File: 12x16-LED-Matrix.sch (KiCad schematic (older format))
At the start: 197 parts, among them J1 Conn_01x16, J2 Conn_01x12

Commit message: Add ground pins, fix silkscreen
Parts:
- removed J1: Conn_01x16, Connector_PinHeader_2.54mm:PinHeader_1x16_P2.54mm_Vertical, symbol Connector_Generic:Conn_01x16
- removed J2: Conn_01x12, Connector_PinHeader_2.54mm:PinHeader_1x12_P2.54mm_Vertical, symbol Connector_Generic:Conn_01x12
- added J1: Conn_01x17, Connector_PinHeader_2.54mm:PinHeader_1x17_P2.54mm_Vertical, symbol Connector_Generic:Conn_01x17
- added J2: Conn_01x13, Connector_PinHeader_2.54mm:PinHeader_1x13_P2.54mm_Vertical, symbol Connector_Generic:Conn_01x13
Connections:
- net at D1.1 (K), D10.1 (K), D11.1 (K)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: now also J2.12 (Pin_12)
- net at D114.2 (A), D130.2 (A), D146.2 (A)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: now also J1.2 (Pin_2)
- net at D115.2 (A), D131.2 (A), D147.2 (A)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: now also J1.3 (Pin_3)
- net at D100.2 (A), D116.2 (A), D132.2 (A)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: now also J1.4 (Pin_4)
- net at D101.2 (A), D117.2 (A), D133.2 (A)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: now also J1.5 (Pin_5)
- net at D102.2 (A), D118.2 (A), D134.2 (A)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: now also J1.6 (Pin_6)
- net at D103.2 (A), D119.2 (A), D135.2 (A)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: now also J1.7 (Pin_7)
- net at D104.2 (A), D120.2 (A), D136.2 (A)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: now also J1.8 (Pin_8)
- net at D105.2 (A), D121.2 (A), D137.2 (A)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: now also J1.9 (Pin_9)
- net at D10.2 (A), D106.2 (A), D122.2 (A)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: now also J1.10 (Pin_10)
- net at D107.2 (A), D11.2 (A), D123.2 (A)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: now also J1.11 (Pin_11)
- net at D108.2 (A), D12.2 (A), D124.2 (A)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: now also J1.12 (Pin_12)
- net at D109.2 (A), D125.2 (A), D13.2 (A)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: now also J1.13 (Pin_13)
- net at D110.2 (A), D126.2 (A), D14.2 (A)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: now also J1.14 (Pin_14)
- net at D111.2 (A), D127.2 (A), D143.2 (A)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: now also J1.15 (Pin_15)
- net at D112.2 (A), D128.2 (A), D144.2 (A)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: now also J1.16 (Pin_16)
- net at D1.2 (A), D113.2 (A), D129.2 (A)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: now also J1.1 (Pin_1)
- net at D17.1 (K), D18.1 (K), D19.1 (K)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: now also J2.11 (Pin_11)
- net at D33.1 (K), D34.1 (K), D35.1 (K)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: now also J2.10 (Pin_10)
- net at D49.1 (K), D50.1 (K), D51.1 (K)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: now also J2.9 (Pin_9)
- net at D65.1 (K), D66.1 (K), D67.1 (K)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: now also J2.8 (Pin_8)
- net at D81.1 (K), D82.1 (K), D83.1 (K)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: now also J2.7 (Pin_7)
- net at D100.1 (K), D101.1 (K), D102.1 (K)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: now also J2.6 (Pin_6)
- net at D113.1 (K), D114.1 (K), D115.1 (K)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: now also J2.5 (Pin_5)
- net at D129.1 (K), D130.1 (K), D131.1 (K)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: now also J2.4 (Pin_4)
- net at D145.1 (K), D146.1 (K), D147.1 (K)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: now also J2.3 (Pin_3)
- net at D161.1 (K), D162.1 (K), D163.1 (K)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: now also J2.2 (Pin_2)
- net at D177.1 (K), D178.1 (K), D179.1 (K)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: now also J2.1 (Pin_1)
- new net GND: J1.17 (Pin_17), J2.13 (Pin_13)
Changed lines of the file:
@@
 Wire Wire Line
 	6200 5500 6200 5150
-$Comp
-L Connector_Generic:Conn_01x12 J2
-U 1 1 61F0FCFB
-P 750 2700
-F 0 "J2" H 668 1875 50  0000 C CNN
-F 1 "Conn_01x12" H 668 1966 50  0000 C CNN
-F 2 "Connector_PinHeader_2.54mm:PinHeader_1x12_P2.54mm_Vertical" H 750 2700 50  0001 C CNN
-F 3 "~" H 750 2700 50  0001 C CNN
-	1    750  2700
-	-1   0    0    1
-$EndComp
 Wire Wire Line
 	1500 2450 1450 2450
@@
 	1500 2100 950  2100
 Connection ~ 1500 2100
-$Comp
-L Connector_Generic:Conn_01x16 J1
-U 1 1 62BDBE0D
-P 2400 850
-F 0 "J1" V 2617 796 50  0000 C CNN
-F 1 "Conn_01x16" V 2526 796 50  0000 C CNN
-F 2 "Connector_PinHeader_2.54mm:PinHeader_1x16_P2.54mm_Vertical" H 2400 850 50  0001 C CNN
-F 3 "~" H 2400 850 50  0001 C CNN
-	1    2400 850
-	0    -1   -1   0
-$EndComp
-Wire Wire Line
-	1700 1050 1700 2000
 Wire Wire Line
 	2000 1750 1800 1750
@@
 	5900 1100 3100 1100
 Wire Wire Line
-	3100 1100 3100 1050
-Wire Wire Line
 	5900 1100 5900 2000
 Wire Wire Line
-	6200 1050 3200 1050
-Wire Wire Line
 	6200 1050 6200 2000
-Wire Wire Line
-	3000 1050 3000 1150
-Wire Wire Line
-	2900 1050 2900 1200
-Wire Wire Line
-	2800 1050 2800 1250
-Wire Wire Line
-	2700 1050 2700 1300
-Wire Wire Line
-	2600 1050 2600 1350
-Wire Wire Line
-	2500 1050 2500 1400
-Wire Wire Line
-	2400 1050 2400 1450
-Wire Wire Line
-	2300 1050 2300 1500
-Wire Wire Line
-	2200 1050 2200 1550
-Wire Wire Line
-	2100 1050 2100 1600
-Wire Wire Line
-	2000 1050 2000 1650
-Wire Wire Line
-	1900 1050 1900 1700
-Wire Wire Line
-	1800 1050 1800 1750
 $Comp
 L Mechanical:MountingHole H1
@@
 	1    0    0    -1
 $EndComp
+$Comp
+L Connector_Generic:Conn_01x13 J2
+U 1 1 61961DD2
+P 750 2600
+F 0 "J2" H 668 1775 50  0000 C CNN
+F 1 "Conn_01x13" H 668 1866 50  0000 C CNN
+F 2 "Connector_PinHeader_2.54mm:PinHeader_1x13_P2.54mm_Vertical" H 750 2600 50  0001 C CNN
+F 3 "~" H 750 2600 50  0001 C CNN
+	1    750  2600
+	-1   0    0    1
+$EndComp
+$Comp
+L power:GND #PWR0101
+U 1 1 619641D7
+P 950 2000
+F 0 "#PWR0101" H 950 1750 50  0001 C CNN
+F 1 "GND" V 955 1872 50  0000 R CNN
+F 2 "" H 950 2000 50  0001 C CNN
+F 3 "" H 950 2000 50  0001 C CNN
+	1    950  2000
+	0    -1   -1   0
+$EndComp
+$Comp
+L Connector_Generic:Conn_01x17 J1
+U 1 1 61965EDC
+P 2500 800
+F 0 "J1" V 2717 796 50  0000 C CNN
+F 1 "Conn_01x17" V 2626 796 50  0000 C CNN
+F 2 "Connector_PinHeader_2.54mm:PinHeader_1x17_P2.54mm_Vertical" H 2500 800 50  0001 C CNN
+F 3 "~" H 2500 800 50  0001 C CNN
+	1    2500 800
+	0    -1   -1   0
+$EndComp
+Wire Wire Line
+	3200 1050 3200 1000
+Wire Wire Line
+	3200 1050 6200 1050
+Wire Wire Line
+	3100 1000 3100 1100
+Wire Wire Line
+	3000 1000 3000 1150
+Wire Wire Line
+	2900 1000 2900 1200
+Wire Wire Line
+	2800 1000 2800 1250
+Wire Wire Line
+	2700 1000 2700 1300
+Wire Wire Line
+	2600 1000 2600 1350
+Wire Wire Line
+	2500 1000 2500 1400
+Wire Wire Line
+	2400 1000 2400 1450
+Wire Wire Line
+	2300 1000 2300 1500
+Wire Wire Line
+	2200 1000 2200 1550
+Wire Wire Line
+	2100 1000 2100 1600
+Wire Wire Line
+	2000 1000 2000 1650
+Wire Wire Line
+	1900 1000 1900 1700
+Wire Wire Line
+	1800 1000 1800 1750
+Wire Wire Line
+	1700 1000 1700 2000
+$Comp
+L power:GND #PWR0102
+U 1 1 620A84A1
+P 3300 1000
+F 0 "#PWR0102" H 3300 750 50  0001 C CNN
+F 1 "GND" V 3305 872 50  0000 R CNN
+F 2 "" H 3300 1000 50  0001 C CNN
+F 3 "" H 3300 1000 50  0001 C CNN
+	1    3300 1000
+	0    -1   -1   0
+$EndComp
 $EndSCHEMATC

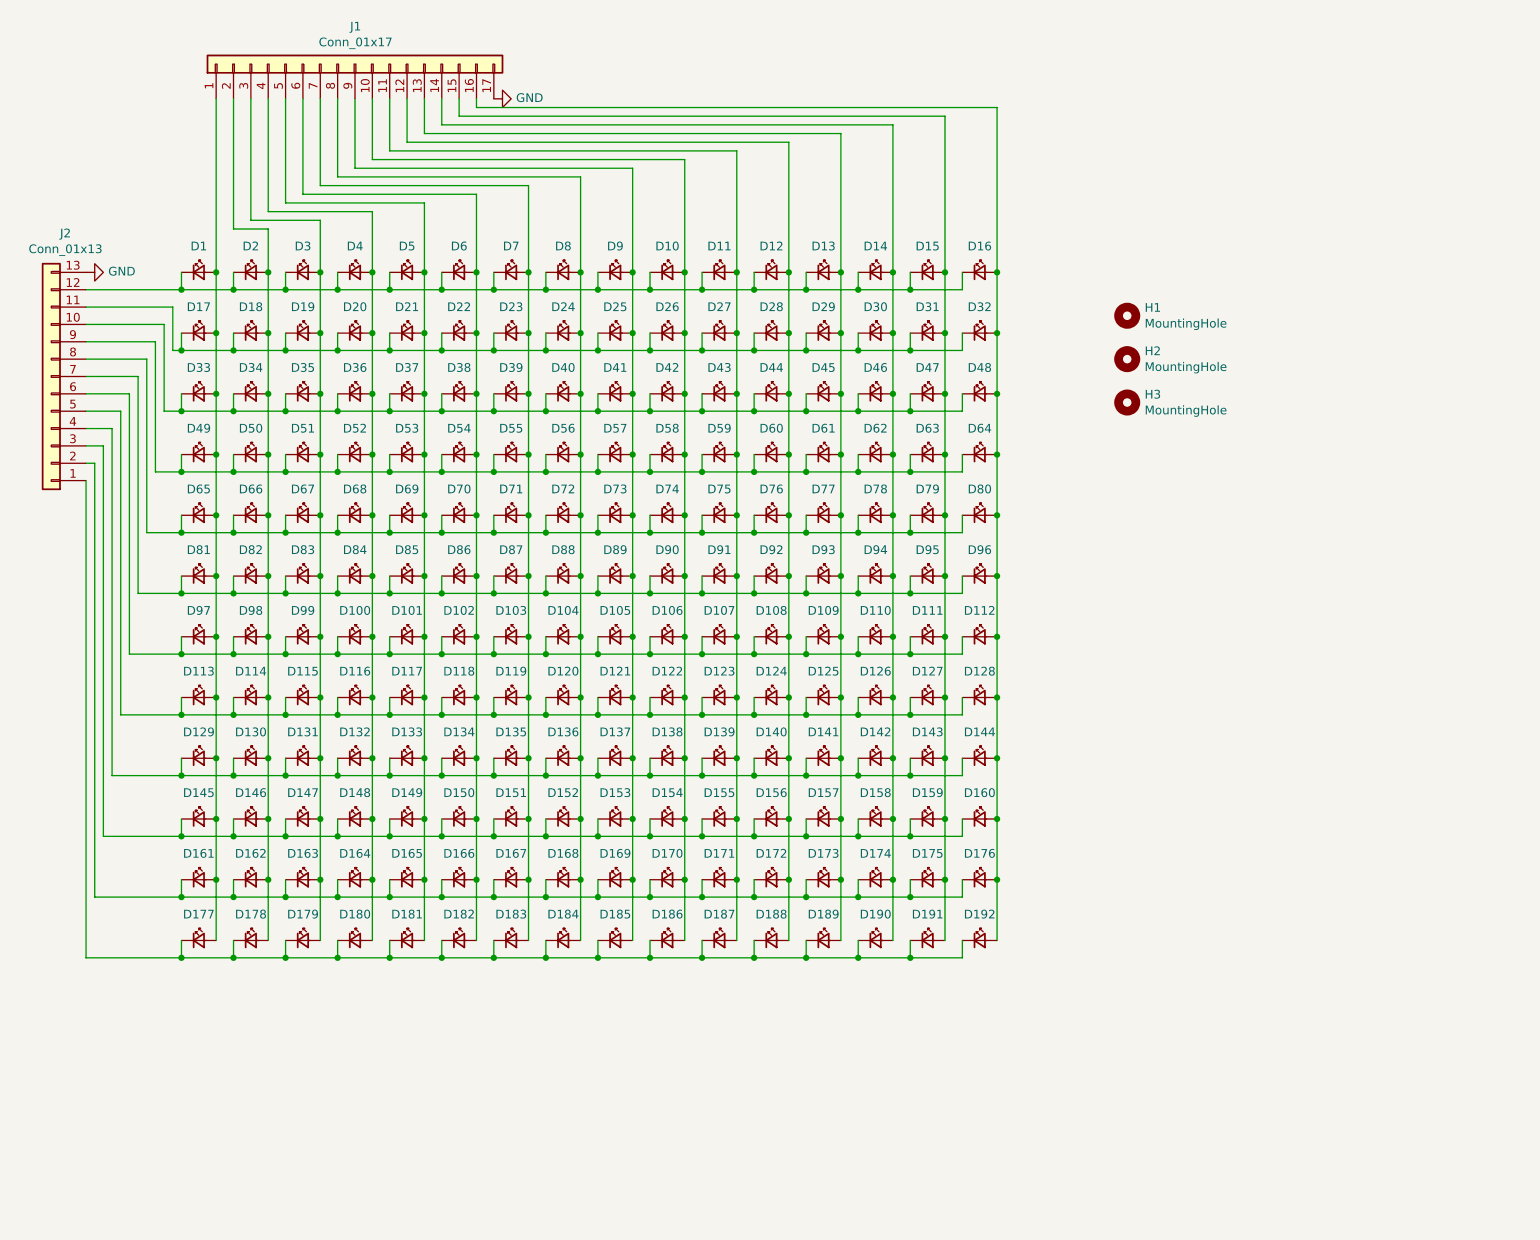
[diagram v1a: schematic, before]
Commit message: Add driver directly to schematic
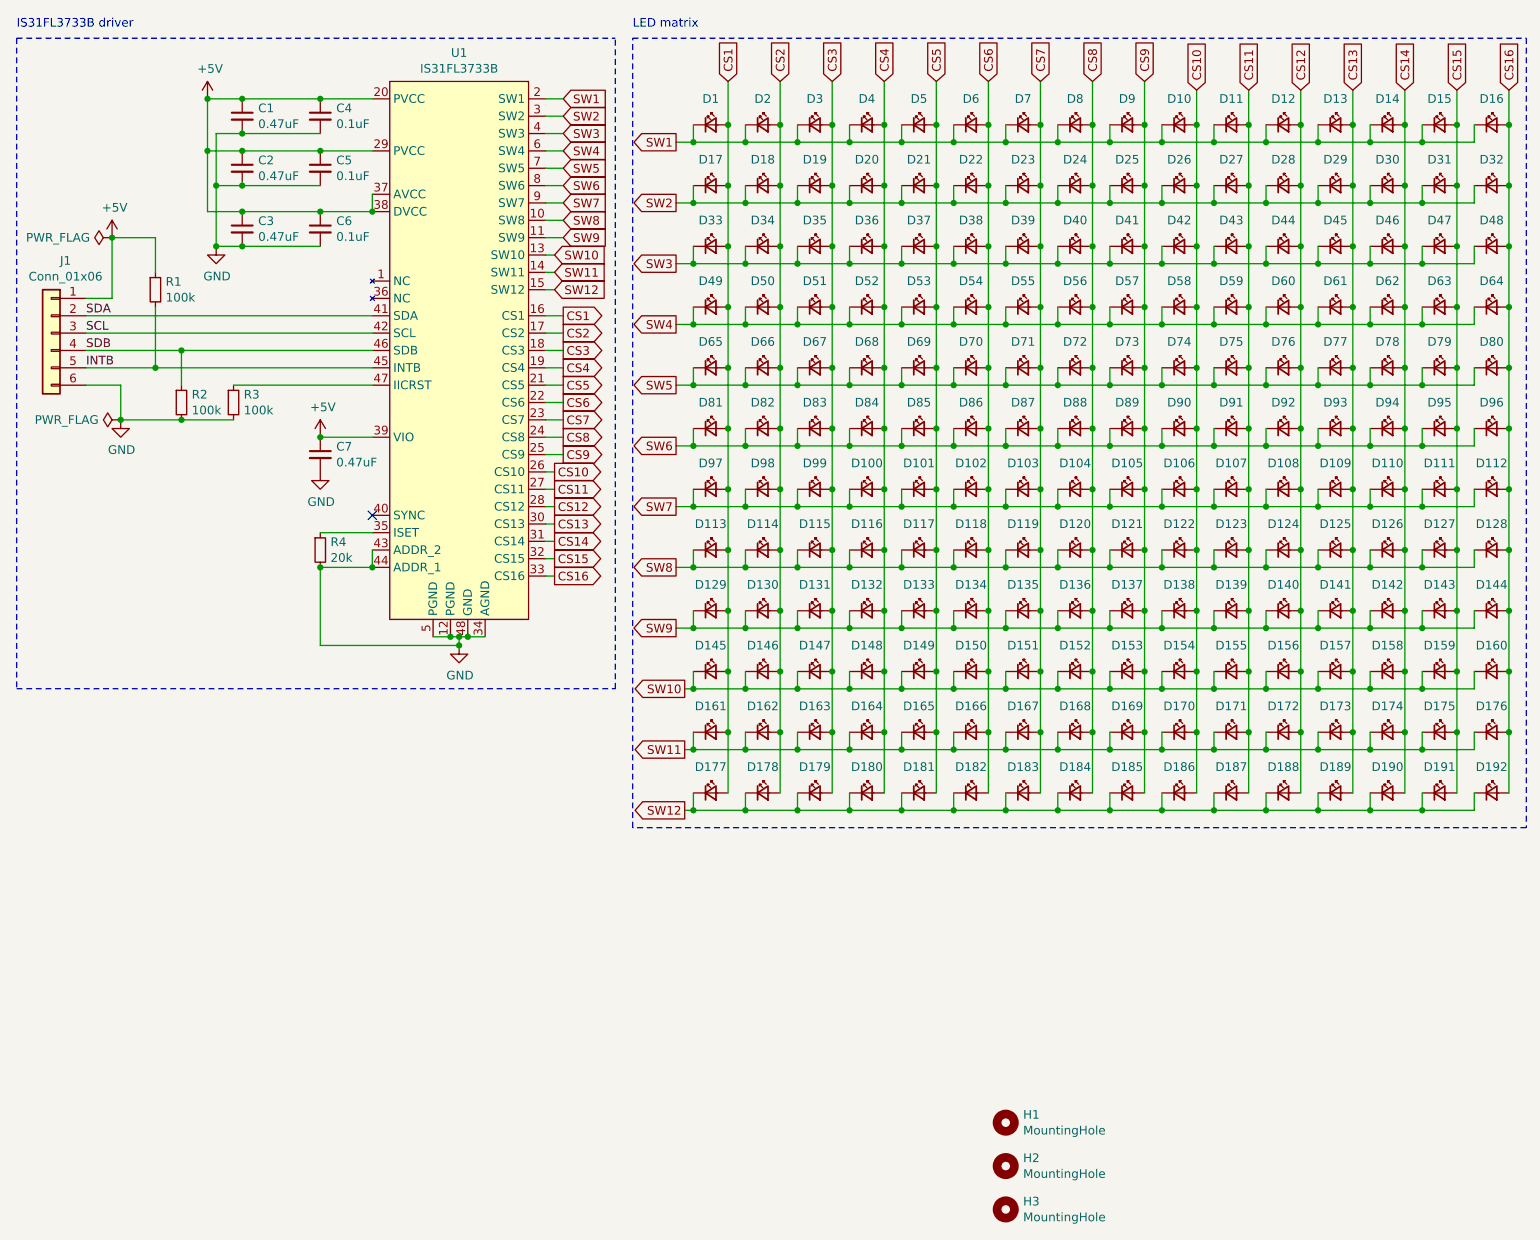
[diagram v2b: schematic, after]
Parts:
- removed J1: Conn_01x17, Connector_PinHeader_2.54mm:PinHeader_1x17_P2.54mm_Vertical, symbol Connector_Generic:Conn_01x17
- removed J2: Conn_01x13, Connector_PinHeader_2.54mm:PinHeader_1x13_P2.54mm_Vertical, symbol Connector_Generic:Conn_01x13
- added C1, C2, C3, C7: 0.47uF, Capacitor_SMD:C_0402_1005Metric, symbol Device:C_Small
- added C4, C5, C6: 0.1uF, Capacitor_SMD:C_0402_1005Metric, symbol Device:C_Small
- added J1: Conn_01x06, Connector_PinHeader_2.54mm:PinHeader_1x06_P2.54mm_Vertical, symbol Connector_Generic:Conn_01x06
- added R1, R2, R3: 100k, Resistor_SMD:R_0402_1005Metric, symbol Device:R_Small
- added R4: 20k, Resistor_SMD:R_0402_1005Metric, symbol Device:R_Small
- added U1: IS31FL3733B, Package_DFN_QFN:QFN-48-1EP_6x6mm_P0.4mm_EP4.3x4.3mm_ThermalVias, symbol 12x16-LED-Matrix:IS31FL3733B
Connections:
- net GND: now also C1.2, C2.2, C3.2, C4.2, C5.2, C6.2, C7.2, J1.6 (Pin_6), R2.2, R3.2, R4.2, U1.12 (PGND), U1.34 (AGND), U1.43 (ADDR_2), U1.44 (ADDR_1), U1.48 (GND), U1.5 (PGND)
- net SW1: now reaches D1.1 (K), D10.1 (K), D11.1 (K), D12.1 (K), D13.1 (K), D14.1 (K), D15.1 (K), D16.1 (K), D2.1 (K), D3.1 (K), D4.1 (K), D5.1 (K), D6.1 (K), D7.1 (K), D8.1 (K), D9.1 (K)
- net SW1: now also U1.2 (SW1)
- net CS2: now reaches D114.2 (A), D130.2 (A), D146.2 (A), D162.2 (A), D178.2 (A), D18.2 (A), D2.2 (A), D34.2 (A), D50.2 (A), D66.2 (A), D82.2 (A), D98.2 (A)
- net CS2: now also U1.17 (CS2)
- net CS3: now reaches D115.2 (A), D131.2 (A), D147.2 (A), D163.2 (A), D179.2 (A), D19.2 (A), D3.2 (A), D35.2 (A), D51.2 (A), D67.2 (A), D83.2 (A), D99.2 (A)
- net CS3: now also U1.18 (CS3)
- net CS4: now reaches D100.2 (A), D116.2 (A), D132.2 (A), D148.2 (A), D164.2 (A), D180.2 (A), D20.2 (A), D36.2 (A), D4.2 (A), D52.2 (A), D68.2 (A), D84.2 (A)
- net CS4: now also U1.19 (CS4)
- net CS5: now reaches D101.2 (A), D117.2 (A), D133.2 (A), D149.2 (A), D165.2 (A), D181.2 (A), D21.2 (A), D37.2 (A), D5.2 (A), D53.2 (A), D69.2 (A), D85.2 (A)
- net CS5: now also U1.21 (CS5)
- net CS6: now reaches D102.2 (A), D118.2 (A), D134.2 (A), D150.2 (A), D166.2 (A), D182.2 (A), D22.2 (A), D38.2 (A), D54.2 (A), D6.2 (A), D70.2 (A), D86.2 (A)
- net CS6: now also U1.22 (CS6)
- net CS7: now reaches D103.2 (A), D119.2 (A), D135.2 (A), D151.2 (A), D167.2 (A), D183.2 (A), D23.2 (A), D39.2 (A), D55.2 (A), D7.2 (A), D71.2 (A), D87.2 (A)
- net CS7: now also U1.23 (CS7)
- net CS8: now reaches D104.2 (A), D120.2 (A), D136.2 (A), D152.2 (A), D168.2 (A), D184.2 (A), D24.2 (A), D40.2 (A), D56.2 (A), D72.2 (A), D8.2 (A), D88.2 (A)
- net CS8: now also U1.24 (CS8)
- net CS9: now reaches D105.2 (A), D121.2 (A), D137.2 (A), D153.2 (A), D169.2 (A), D185.2 (A), D25.2 (A), D41.2 (A), D57.2 (A), D73.2 (A), D89.2 (A), D9.2 (A)
- net CS9: now also U1.25 (CS9)
- net CS10: now reaches D10.2 (A), D106.2 (A), D122.2 (A), D138.2 (A), D154.2 (A), D170.2 (A), D186.2 (A), D26.2 (A), D42.2 (A), D58.2 (A), D74.2 (A), D90.2 (A)
- net CS10: now also U1.26 (CS10)
- net CS11: now reaches D107.2 (A), D11.2 (A), D123.2 (A), D139.2 (A), D155.2 (A), D171.2 (A), D187.2 (A), D27.2 (A), D43.2 (A), D59.2 (A), D75.2 (A), D91.2 (A)
- net CS11: now also U1.27 (CS11)
- net CS12: now reaches D108.2 (A), D12.2 (A), D124.2 (A), D140.2 (A), D156.2 (A), D172.2 (A), D188.2 (A), D28.2 (A), D44.2 (A), D60.2 (A), D76.2 (A), D92.2 (A)
- net CS12: now also U1.28 (CS12)
- net CS13: now reaches D109.2 (A), D125.2 (A), D13.2 (A), D141.2 (A), D157.2 (A), D173.2 (A), D189.2 (A), D29.2 (A), D45.2 (A), D61.2 (A), D77.2 (A), D93.2 (A)
- net CS13: now also U1.30 (CS13)
- net CS14: now reaches D110.2 (A), D126.2 (A), D14.2 (A), D142.2 (A), D158.2 (A), D174.2 (A), D190.2 (A), D30.2 (A), D46.2 (A), D62.2 (A), D78.2 (A), D94.2 (A)
- net CS14: now also U1.31 (CS14)
- net CS15: now reaches D111.2 (A), D127.2 (A), D143.2 (A), D15.2 (A), D159.2 (A), D175.2 (A), D191.2 (A), D31.2 (A), D47.2 (A), D63.2 (A), D79.2 (A), D95.2 (A)
- net CS15: now also U1.32 (CS15)
- net CS16: now reaches D112.2 (A), D128.2 (A), D144.2 (A), D16.2 (A), D160.2 (A), D176.2 (A), D192.2 (A), D32.2 (A), D48.2 (A), D64.2 (A), D80.2 (A), D96.2 (A)
- net CS16: now also U1.33 (CS16)
- net CS1: now reaches D1.2 (A), D113.2 (A), D129.2 (A), D145.2 (A), D161.2 (A), D17.2 (A), D177.2 (A), D33.2 (A), D49.2 (A), D65.2 (A), D81.2 (A), D97.2 (A)
- net CS1: now also U1.16 (CS1)
- net SW2: now reaches D17.1 (K), D18.1 (K), D19.1 (K), D20.1 (K), D21.1 (K), D22.1 (K), D23.1 (K), D24.1 (K), D25.1 (K), D26.1 (K), D27.1 (K), D28.1 (K), D29.1 (K), D30.1 (K), D31.1 (K), D32.1 (K)
- net SW2: now also U1.3 (SW2)
- net SW3: now reaches D33.1 (K), D34.1 (K), D35.1 (K), D36.1 (K), D37.1 (K), D38.1 (K), D39.1 (K), D40.1 (K), D41.1 (K), D42.1 (K), D43.1 (K), D44.1 (K), D45.1 (K), D46.1 (K), D47.1 (K), D48.1 (K)
- net SW3: now also U1.4 (SW3)
- net SW4: now reaches D49.1 (K), D50.1 (K), D51.1 (K), D52.1 (K), D53.1 (K), D54.1 (K), D55.1 (K), D56.1 (K), D57.1 (K), D58.1 (K), D59.1 (K), D60.1 (K), D61.1 (K), D62.1 (K), D63.1 (K), D64.1 (K)
- net SW4: now also U1.6 (SW4)
- net SW5: now reaches D65.1 (K), D66.1 (K), D67.1 (K), D68.1 (K), D69.1 (K), D70.1 (K), D71.1 (K), D72.1 (K), D73.1 (K), D74.1 (K), D75.1 (K), D76.1 (K), D77.1 (K), D78.1 (K), D79.1 (K), D80.1 (K)
- net SW5: now also U1.7 (SW5)
- net SW6: now reaches D81.1 (K), D82.1 (K), D83.1 (K), D84.1 (K), D85.1 (K), D86.1 (K), D87.1 (K), D88.1 (K), D89.1 (K), D90.1 (K), D91.1 (K), D92.1 (K), D93.1 (K), D94.1 (K), D95.1 (K), D96.1 (K)
- net SW6: now also U1.8 (SW6)
- net SW12: now reaches D177.1 (K), D178.1 (K), D179.1 (K), D180.1 (K), D181.1 (K), D182.1 (K), D183.1 (K), D184.1 (K), D185.1 (K), D186.1 (K), D187.1 (K), D188.1 (K), D189.1 (K), D190.1 (K), D191.1 (K), D192.1 (K)
- net SW12: now also U1.15 (SW12)
- net SW11: now reaches D161.1 (K), D162.1 (K), D163.1 (K), D164.1 (K), D165.1 (K), D166.1 (K), D167.1 (K), D168.1 (K), D169.1 (K), D170.1 (K), D171.1 (K), D172.1 (K), D173.1 (K), D174.1 (K), D175.1 (K), D176.1 (K)
- net SW11: now also U1.14 (SW11)
- net SW10: now reaches D145.1 (K), D146.1 (K), D147.1 (K), D148.1 (K), D149.1 (K), D150.1 (K), D151.1 (K), D152.1 (K), D153.1 (K), D154.1 (K), D155.1 (K), D156.1 (K), D157.1 (K), D158.1 (K), D159.1 (K), D160.1 (K)
- net SW10: now also U1.13 (SW10)
- net SW9: now reaches D129.1 (K), D130.1 (K), D131.1 (K), D132.1 (K), D133.1 (K), D134.1 (K), D135.1 (K), D136.1 (K), D137.1 (K), D138.1 (K), D139.1 (K), D140.1 (K), D141.1 (K), D142.1 (K), D143.1 (K), D144.1 (K)
- net SW9: now also U1.11 (SW9)
- net SW8: now reaches D113.1 (K), D114.1 (K), D115.1 (K), D116.1 (K), D117.1 (K), D118.1 (K), D119.1 (K), D120.1 (K), D121.1 (K), D122.1 (K), D123.1 (K), D124.1 (K), D125.1 (K), D126.1 (K), D127.1 (K), D128.1 (K)
- net SW8: now also U1.10 (SW8)
- net SW7: now reaches D100.1 (K), D101.1 (K), D102.1 (K), D103.1 (K), D104.1 (K), D105.1 (K), D106.1 (K), D107.1 (K), D108.1 (K), D109.1 (K), D110.1 (K), D111.1 (K), D112.1 (K), D97.1 (K), D98.1 (K), D99.1 (K)
- net SW7: now also U1.9 (SW7)
- new net: R4.1, U1.35 (ISET)
- new net: R3.1, U1.47 (IICRST)
- new net +5V: C1.1, C2.1, C3.1, C4.1, C5.1, C6.1, C7.1, J1.1 (Pin_1), R1.1, U1.20 (PVCC), U1.29 (PVCC), U1.37 (AVCC), U1.38 (DVCC), U1.39 (VIO)
- new net INTB: J1.5 (Pin_5), R1.2, U1.45 (INTB)
- new net SCL: J1.3 (Pin_3), U1.42 (SCL)
- new net SDA: J1.2 (Pin_2), U1.41 (SDA)
- new net SDB: J1.4 (Pin_4), R2.1, U1.46 (SDB)
- no-connect marks 0 -> 1
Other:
- note added: "IS31FL3733B driver"
- note added: "LED matrix"
- moved on the sheet: D1, D10, D100, D101, D102, D103, D104, D105, D106, D107, D108, D109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

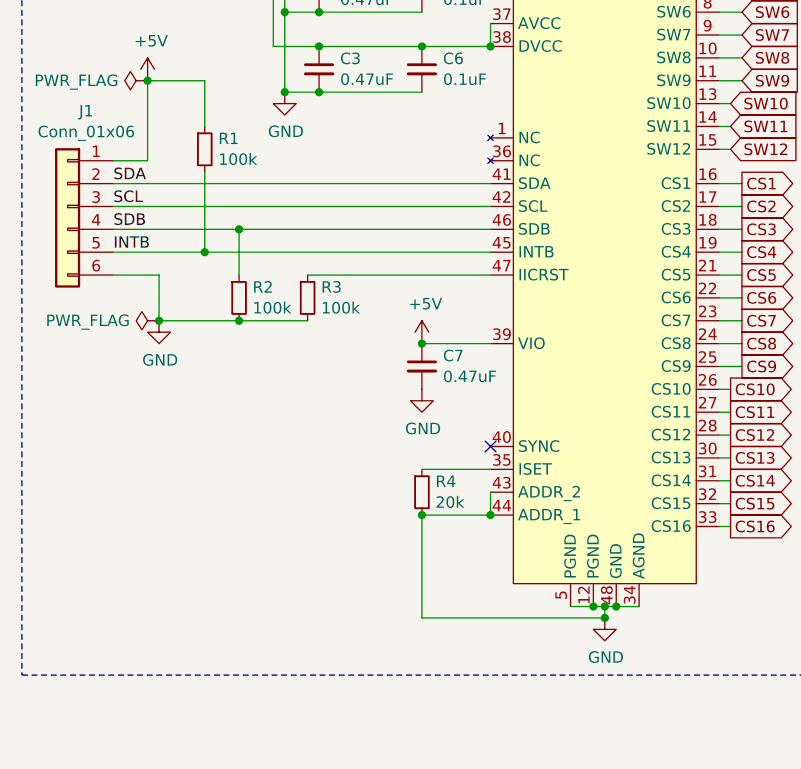
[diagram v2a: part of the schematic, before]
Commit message: Fully routed board
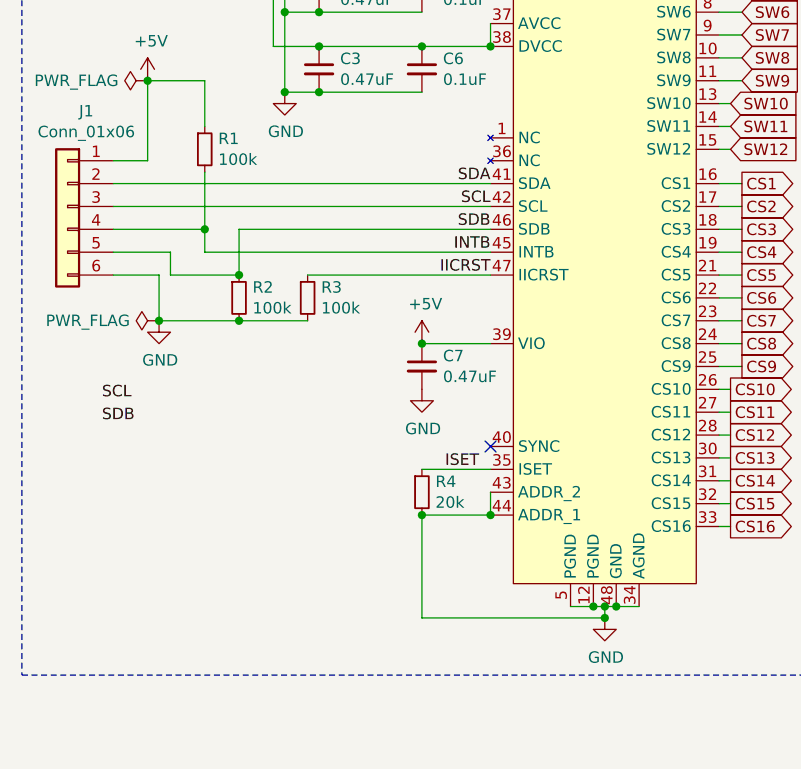
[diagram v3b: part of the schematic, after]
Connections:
- net INTB: now also J1.4 (Pin_4); no longer J1.5 (Pin_5)
- net SDB: now also J1.5 (Pin_5); no longer J1.4 (Pin_4)
- net ISET: now reaches R4.1, U1.35 (ISET)
- net IICRST: now reaches R3.1, U1.47 (IICRST)
